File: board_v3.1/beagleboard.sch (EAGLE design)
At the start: 32 parts, among them U1 DWM1000

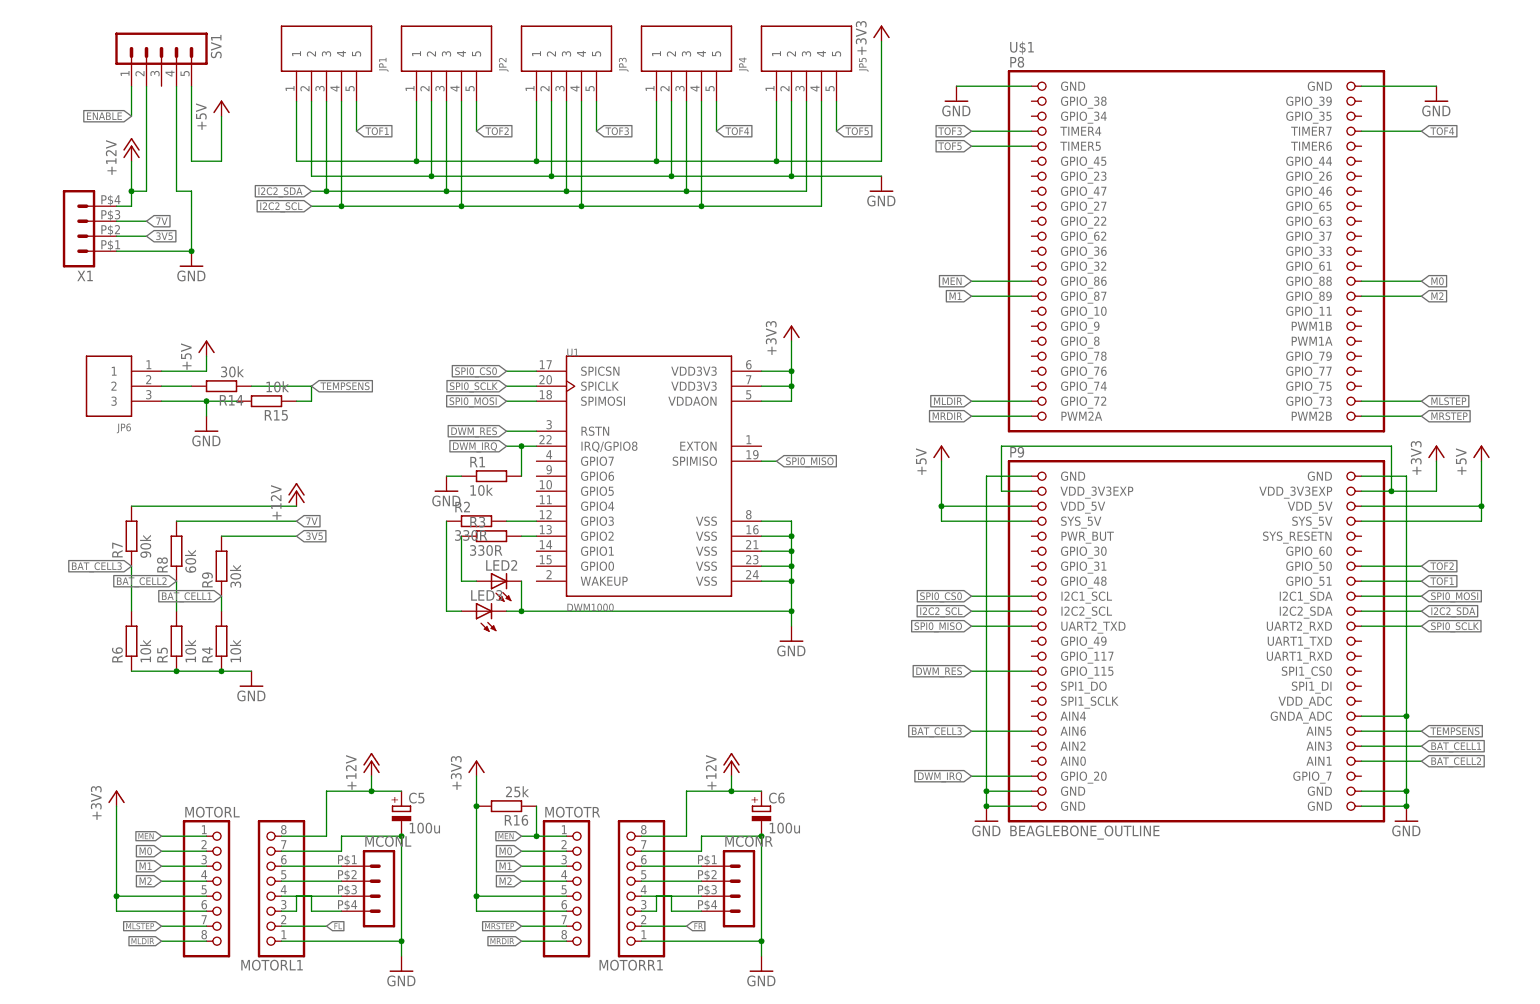
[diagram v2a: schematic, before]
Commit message: board v3.1 beta 7: replaced DWM1000 module with connector for dwm1000-addon board, redone battery cell voltage routes. No more vias.
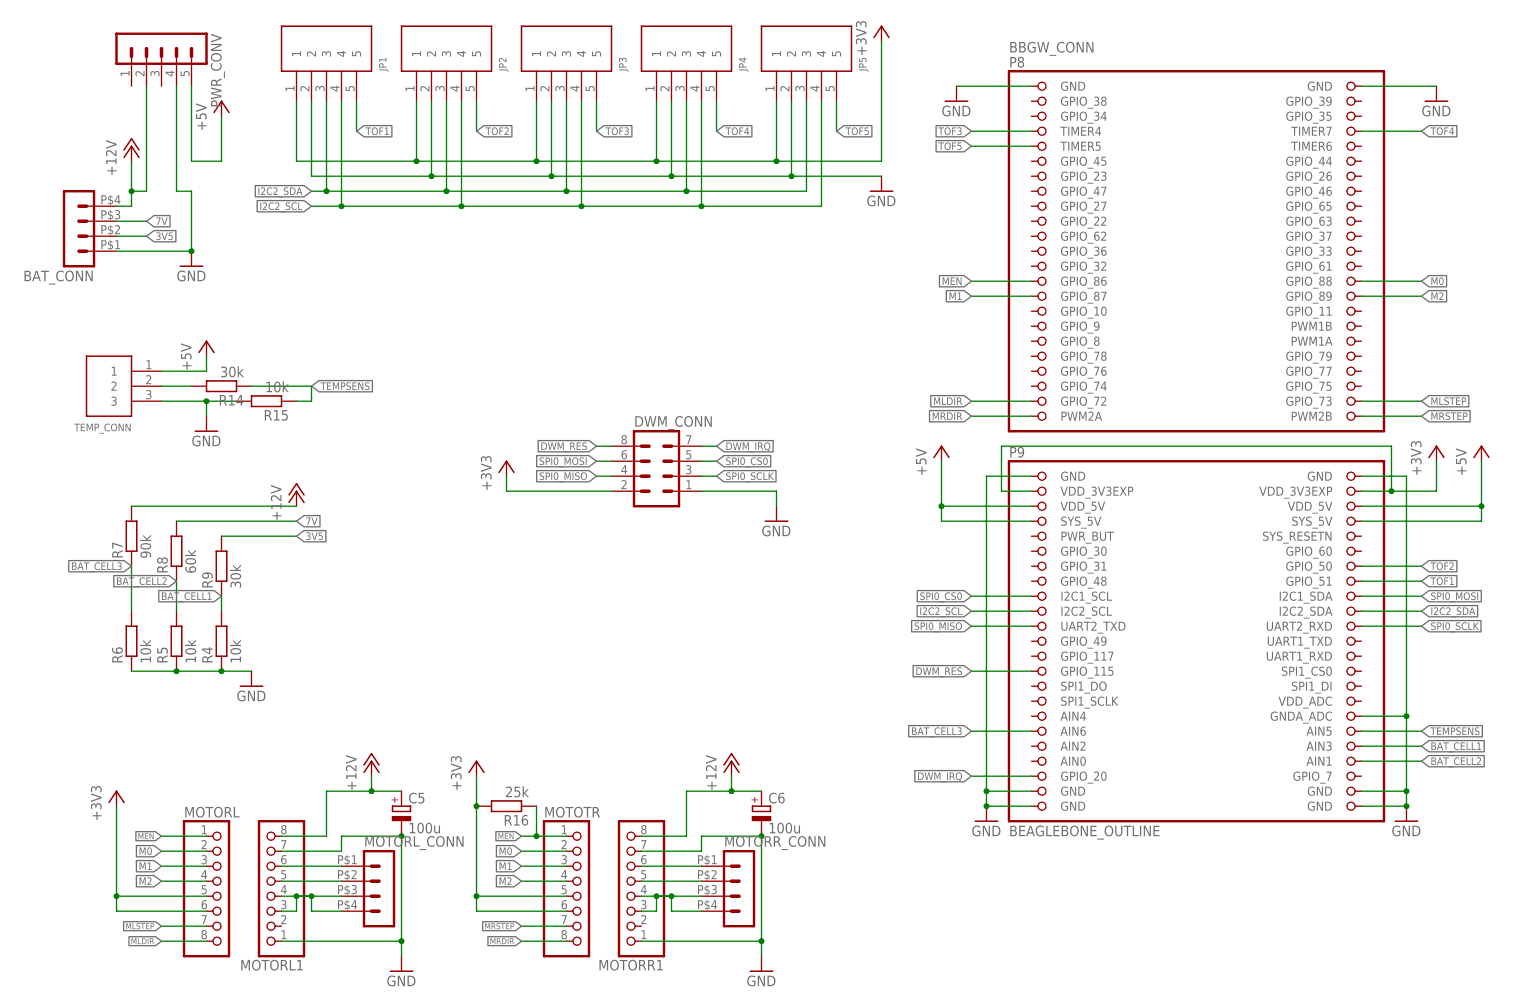
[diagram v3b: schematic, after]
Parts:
- removed LED2, LED3: (no value), led:LEDSML0603
- removed R1: 10k, rcl:R-EU_R0603
- removed R2, R3: 330R, rcl:R-EU_R0603
- removed U1: DWM1000, DWM1000:DWM1000
- added DWM_CONN: (no value), con-lstb:MA04-2
- renumbered JP6 to TEMP_CONN, MCONL to MOTORL_CONN, MCONR to MOTORR_CONN, SV1 to PWR_CONV, U$1 to BBGW_CONN, X1 to BAT_CONN
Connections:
- removed net ENABLE: PWR_CONV.1
- removed net FL: MOTORL1.2
- removed net FR: MOTORR1.2
- removed net N$11: MOTORL1.3, MOTORL_CONN.3
- removed net N$15: MOTORR1.3, MOTORR_CONN.3
- removed net N$2: R3.2, U1.GPIO2
- removed net N$3: R2.2, U1.GPIO3
- removed net N$5: LED2.A, R3.1
- removed net N$6: LED3.A, R2.1
- net +3V3: now also DWM_CONN.2; no longer U1.VDD3V3@1, U1.VDD3V3@2, U1.VDDAON
- net DWM_IRQ: now also DWM_CONN.7; no longer R1.2, U1.IRQ/GPIO8
- net DWM_RES: now also DWM_CONN.8; no longer U1.RSTN
- net GND: now also DWM_CONN.1; no longer LED2.C, LED3.C, R1.1, U1.VSS@1, U1.VSS@2, U1.VSS@3, U1.VSS@4, U1.VSS@5
- net N$1: now also MOTORL1.3, MOTORL_CONN.3
- net N$14: now also MOTORR1.3, MOTORR_CONN.3
- net SPI0_CS0: now also DWM_CONN.5; no longer U1.SPICSN
- net SPI0_MISO: now also DWM_CONN.4; no longer U1.SPIMISO
- net SPI0_MOSI: now also DWM_CONN.6; no longer U1.SPIMOSI
- net SPI0_SCLK: now also DWM_CONN.3; no longer U1.SPICLK

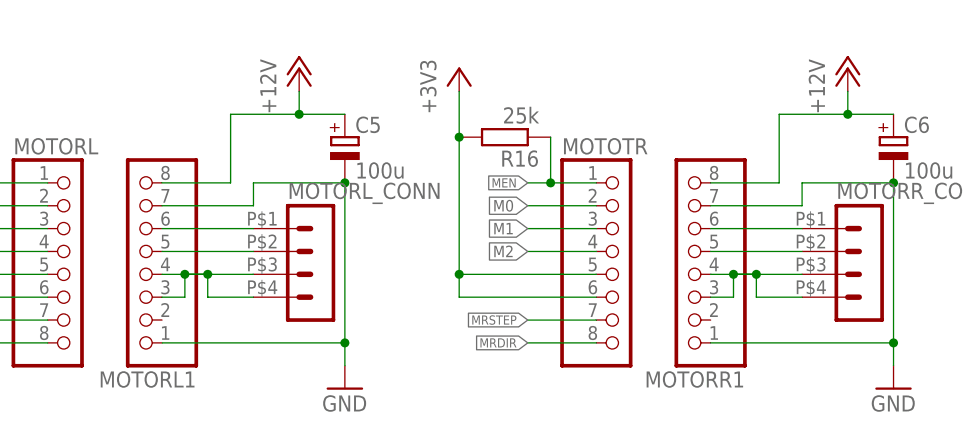
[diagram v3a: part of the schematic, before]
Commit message: board v3.1 beta 7: fixed bad networks between motor drivers and connectors; fixed some clearance issues
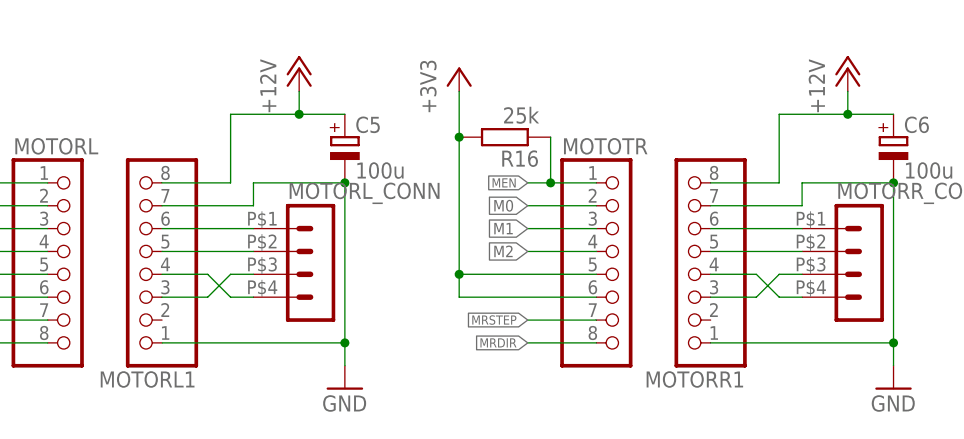
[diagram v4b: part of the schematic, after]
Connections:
- removed net N$14: MOTORR1.3, MOTORR1.4, MOTORR_CONN.3, MOTORR_CONN.4
- new net N$2: MOTORL1.4, MOTORL_CONN.4
- new net N$3: MOTORR1.3, MOTORR_CONN.3
- new net N$4: MOTORR1.4, MOTORR_CONN.4
- net N$1: no longer MOTORL1.4, MOTORL_CONN.4
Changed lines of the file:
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@@
-</segment>
-</net>
-<net name="N$1" class="0">
-<segment>
-<pinref part="MOTORL1" gate="A" pin="4"/>
-<wire x1="12.7" y1="-17.78" x2="15.24" y2="-17.78" width="0.1524" layer="91"/>
-<wire x1="15.24" y1="-17.78" x2="17.78" y2="-17.78" width="0.1524" layer="91"/>
-<wire x1="17.78" y1="-17.78" x2="17.78" y2="-20.32" width="0.1524" layer="91"/>
-<pinref part="MOTORL_CONN" gate="G$1" pin="4"/>
-<wire x1="17.78" y1="-20.32" x2="22.86" y2="-20.32" width="0.1524" layer="91"/>
-<pinref part="MOTORL_CONN" gate="G$1" pin="3"/>
-<wire x1="22.86" y1="-17.78" x2="17.78" y2="-17.78" width="0.1524" layer="91"/>
-<wire x1="17.78" y1="-17.78" x2="15.24" y2="-17.78" width="0.1524" layer="91"/>
-<wire x1="15.24" y1="-17.78" x2="15.24" y2="-20.32" width="0.1524" layer="91"/>
-<pinref part="MOTORL1" gate="A" pin="3"/>
-<wire x1="15.24" y1="-20.32" x2="12.7" y2="-20.32" width="0.1524" layer="91"/>
-<junction x="15.24" y="-17.78"/>
-<junction x="17.78" y="-17.78"/>
 </segment>
 </net>
@@
 <pinref part="MOTORR_CONN" gate="G$1" pin="2"/>
 <wire x1="73.66" y1="-15.24" x2="83.82" y2="-15.24" width="0.1524" layer="91"/>
-</segment>
-</net>
-<net name="N$14" class="0">
-<segment>
-<pinref part="MOTORR1" gate="A" pin="4"/>
-<wire x1="73.66" y1="-17.78" x2="76.2" y2="-17.78" width="0.1524" layer="91"/>
-<wire x1="76.2" y1="-17.78" x2="78.74" y2="-17.78" width="0.1524" layer="91"/>
-<wire x1="78.74" y1="-17.78" x2="78.74" y2="-20.32" width="0.1524" layer="91"/>
-<pinref part="MOTORR_CONN" gate="G$1" pin="4"/>
-<wire x1="78.74" y1="-20.32" x2="83.82" y2="-20.32" width="0.1524" layer="91"/>
-<pinref part="MOTORR_CONN" gate="G$1" pin="3"/>
-<wire x1="83.82" y1="-17.78" x2="78.74" y2="-17.78" width="0.1524" layer="91"/>
-<wire x1="78.74" y1="-17.78" x2="76.2" y2="-17.78" width="0.1524" layer="91"/>
-<wire x1="76.2" y1="-17.78" x2="76.2" y2="-20.32" width="0.1524" layer="91"/>
-<pinref part="MOTORR1" gate="A" pin="3"/>
-<wire x1="76.2" y1="-20.32" x2="73.66" y2="-20.32" width="0.1524" layer="91"/>
-<junction x="76.2" y="-17.78"/>
-<junction x="78.74" y="-17.78"/>
 </segment>
 </net>
@@
 </segment>
 </net>
+<net name="N$1" class="0">
+<segment>
+<pinref part="MOTORL1" gate="A" pin="3"/>
+<wire x1="12.7" y1="-20.32" x2="17.78" y2="-20.32" width="0.1524" layer="91"/>
+<wire x1="17.78" y1="-20.32" x2="20.32" y2="-17.78" width="0.1524" layer="91"/>
+<pinref part="MOTORL_CONN" gate="G$1" pin="3"/>
+<wire x1="20.32" y1="-17.78" x2="22.86" y2="-17.78" width="0.1524" layer="91"/>
+</segment>
+</net>
+<net name="N$2" class="0">
+<segment>
+<pinref part="MOTORL_CONN" gate="G$1" pin="4"/>
+<wire x1="22.86" y1="-20.32" x2="20.32" y2="-20.32" width="0.1524" layer="91"/>
+<wire x1="20.32" y1="-20.32" x2="17.78" y2="-17.78" width="0.1524" layer="91"/>
+<pinref part="MOTORL1" gate="A" pin="4"/>
+<wire x1="17.78" y1="-17.78" x2="12.7" y2="-17.78" width="0.1524" layer="91"/>
+</segment>
+</net>
+<net name="N$3" class="0">
+<segment>
+<pinref part="MOTORR1" gate="A" pin="3"/>
+<wire x1="73.66" y1="-20.32" x2="78.74" y2="-20.32" width="0.1524" layer="91"/>
+<wire x1="78.74" y1="-20.32" x2="81.28" y2="-17.78" width="0.1524" layer="91"/>
+<pinref part="MOTORR_CONN" gate="G$1" pin="3"/>
+<wire x1="81.28" y1="-17.78" x2="83.82" y2="-17.78" width="0.1524" layer="91"/>
+</segment>
+</net>
+<net name="N$4" class="0">
+<segment>
+<pinref part="MOTORR_CONN" gate="G$1" pin="4"/>
+<wire x1="83.82" y1="-20.32" x2="81.28" y2="-20.32" width="0.1524" layer="91"/>
+<wire x1="81.28" y1="-20.32" x2="78.74" y2="-17.78" width="0.1524" layer="91"/>
+<pinref part="MOTORR1" gate="A" pin="4"/>
+<wire x1="78.74" y1="-17.78" x2="73.66" y2="-17.78" width="0.1524" layer="91"/>
+</segment>
+</net>
 </nets>
 </sheet>
 </sheets>
+<errors>
+</errors>
 </schematic>
 </drawing>

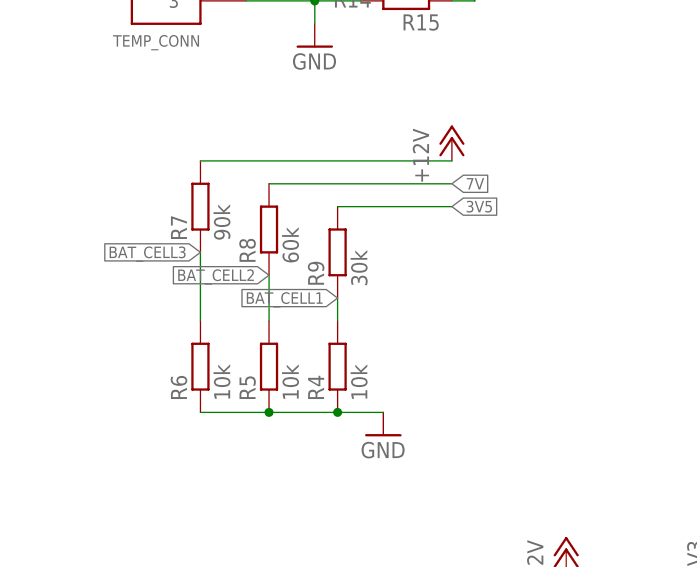
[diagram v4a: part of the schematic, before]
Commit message: board3.1: updated resistors on voltage divider for power
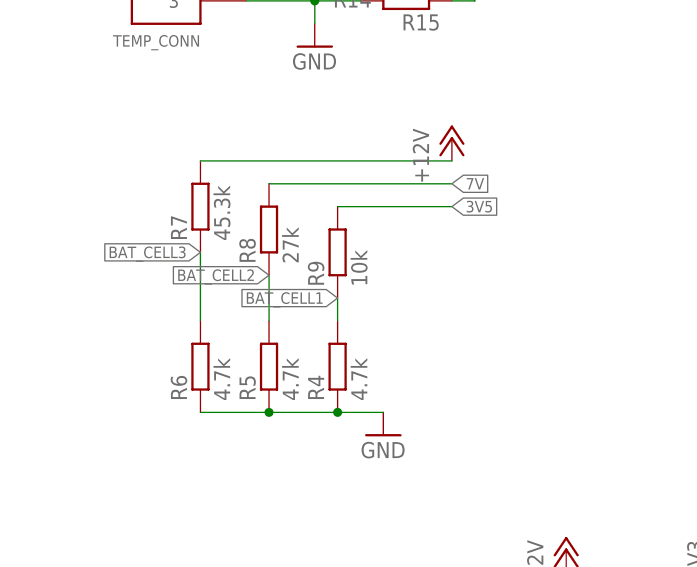
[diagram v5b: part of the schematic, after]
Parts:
- R4, R5, R6: value 10k -> 4.7k
- R7: value 90k -> 45.3k
- R8: value 60k -> 27k
- R9: value 30k -> 10k
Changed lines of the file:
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@@
 <?xml version="1.0" encoding="utf-8"?>
 <!DOCTYPE eagle SYSTEM "eagle.dtd">
-<eagle version="8.2.2">
+<eagle version="8.4.0">
 <drawing>
 <settings>
 <setting alwaysvectorfont="no"/>
+<setting keepoldvectorfont="yes"/>
 <setting verticaltext="up"/>
 </settings>
@@
 <part name="P+6" library="supply1" deviceset="+5V" device=""/>
 <part name="GND13" library="supply1" deviceset="GND" device=""/>
-<part name="R4" library="rcl" deviceset="R-EU_" device="R0603" value="10k"/>
-<part name="R5" library="rcl" deviceset="R-EU_" device="R0603" value="10k"/>
-<part name="R6" library="rcl" deviceset="R-EU_" device="R0603" value="10k"/>
-<part name="R7" library="rcl" deviceset="R-EU_" device="R0603" value="90k"/>
-<part name="R8" library="rcl" deviceset="R-EU_" device="R0603" value="60k"/>
-<part name="R9" library="rcl" deviceset="R-EU_" device="R0603" value="30k"/>
+<part name="R4" library="rcl" deviceset="R-EU_" device="R0603" value="4.7k"/>
+<part name="R5" library="rcl" deviceset="R-EU_" device="R0603" value="4.7k"/>
+<part name="R6" library="rcl" deviceset="R-EU_" device="R0603" value="4.7k"/>
+<part name="R7" library="rcl" deviceset="R-EU_" device="R0603" value="45.3k"/>
+<part name="R8" library="rcl" deviceset="R-EU_" device="R0603" value="27k"/>
+<part name="R9" library="rcl" deviceset="R-EU_" device="R0603" value="10k"/>
 <part name="P+8" library="supply1" deviceset="+5V" device=""/>
 <part name="PWR_CONV" library="con-lstb" deviceset="MA05-1" device=""/>
@@
 <compatibility>
 <note version="8.2" severity="warning">
-Since Version 8.2, Eagle supports online libraries. The ids
+Since Version 8.2, EAGLE supports online libraries. The ids
 of those online libraries will not be understood (or retained)
 with this version.
